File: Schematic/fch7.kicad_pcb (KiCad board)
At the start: 4 copper layers, 39.8 x 41.5 mm, 145 parts, among them IC1 MP9943AGQ-Z, IC2 MP9943AGQ-Z, IC4 ICM-42688-P, IC5 MPU-6500, J11 PIN2216, J12 PIN2216, J2 PIN2216, J3 PIN2216, J4 PIN2216, J5 PIN2216, J6 PIN2216, J7 PIN2216, J8 PIN2216, J9 PIN2216, U1 ME6217C33M5G, U10 HDGC1002WR-S-4P, U11 HDGC1002WR-S-4P, U12 E28-2G4M27SX, U13 STM32H742VIHx, U15 HDGC1002WR-S-6P, U16 HDGC1002WR-S-8P, U17 HDGC1002WR-S-8P, U2 ME6217C33M5G, U3 LDO-1.8v, U4 QMC5883L, U5 SPL06-001, U6 CSNP1GCR01-BOW, U7 HDGC1002WR-S-6P, U8 HDGC1002WR-S-4P, U9 HDGC1002WR-S-4P, Y1 8MHz

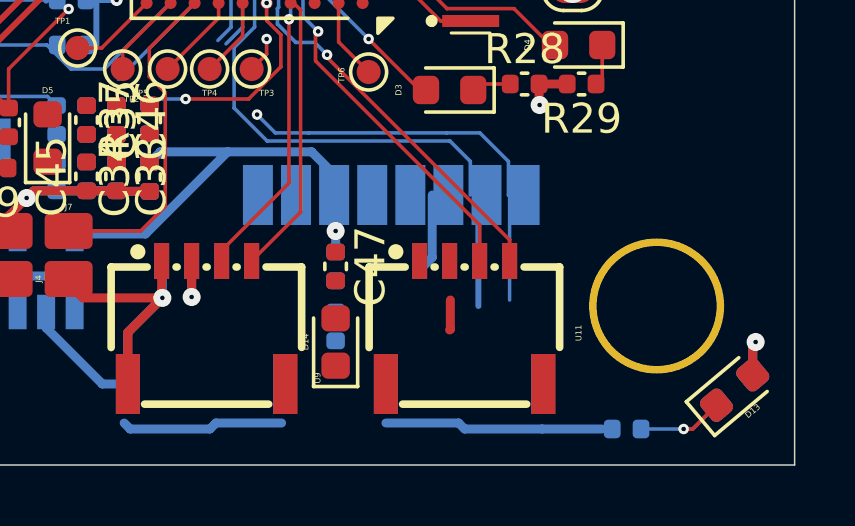
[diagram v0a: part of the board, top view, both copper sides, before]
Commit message: Update schematic files and footprint references
- Updated the footprint reference in `fp-info-cache` for various components to use "fch7" instead of "fch7_fp".
- Added a new 3D library reference for "fch7_3d" in `fp-lib-table`.
- Introduced a new symbol for the RF GPS module "MIA-M10Q" in `rf_rx.kicad_sch`, including properties such as footprint, datasheet, and description.
- Added multiple pins for the "MIA-M10Q" symbol with unique UUIDs.
- Corrected the URI for the `fclib` in `sym-lib-table` to point to the correct project path.
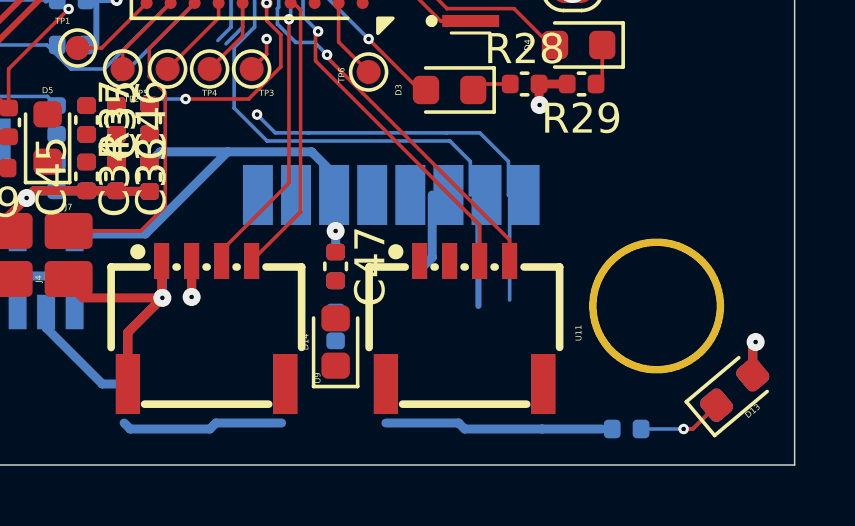
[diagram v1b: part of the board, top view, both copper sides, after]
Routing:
- net 5V: track 37.2 -> 36.2 mm
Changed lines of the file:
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@@
-	)
-	(segment
-		(start 92.724967 97.175033)
-		(end 92.7 97.2)
-		(width 0.3)
-		(layer "F.Cu")
-		(net 9)
 	)
 	(segment
@@
 		(layer "F.Cu")
 		(net 9)
-	)
-	(segment
-		(start 92.724967 96.2)
-		(end 92.724967 97.175033)
-		(width 0.3)
-		(layer "F.Cu")
-		(net 9)

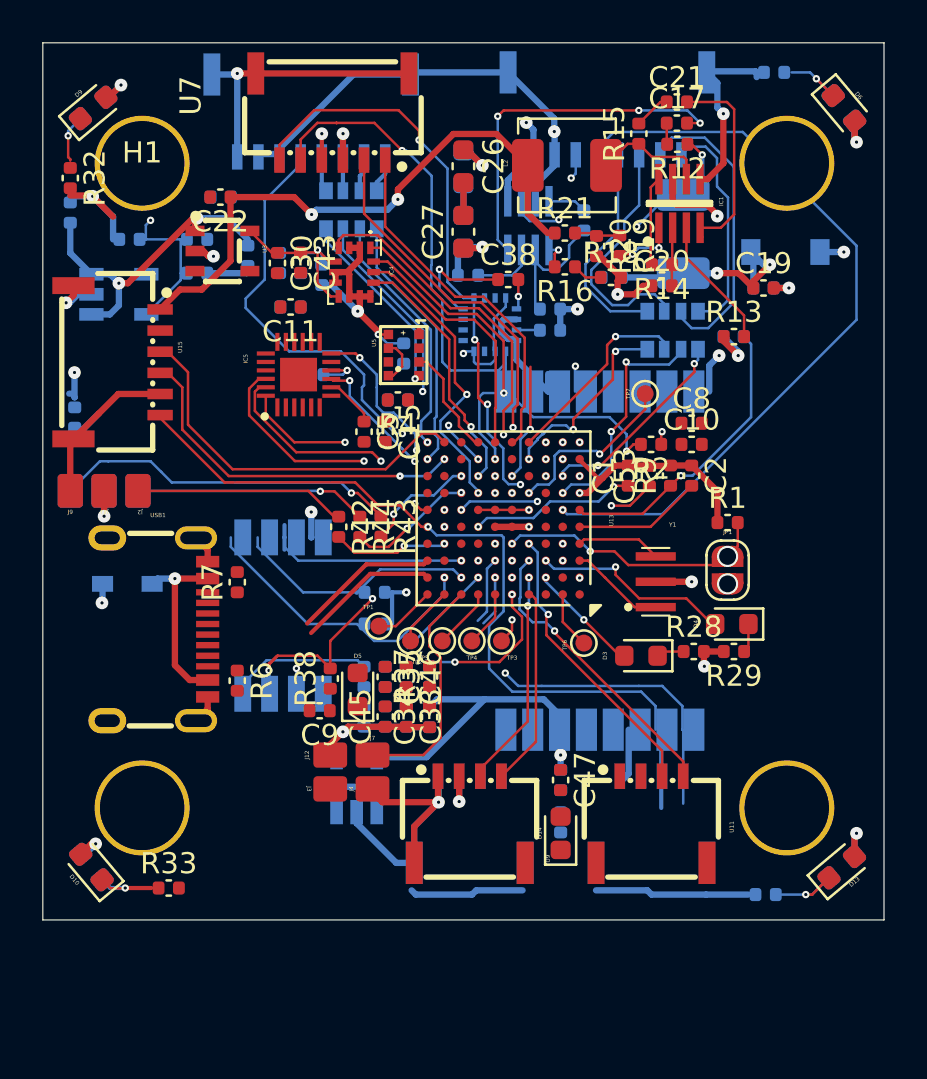
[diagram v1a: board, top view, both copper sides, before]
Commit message: update routing and add MIA-M10Q
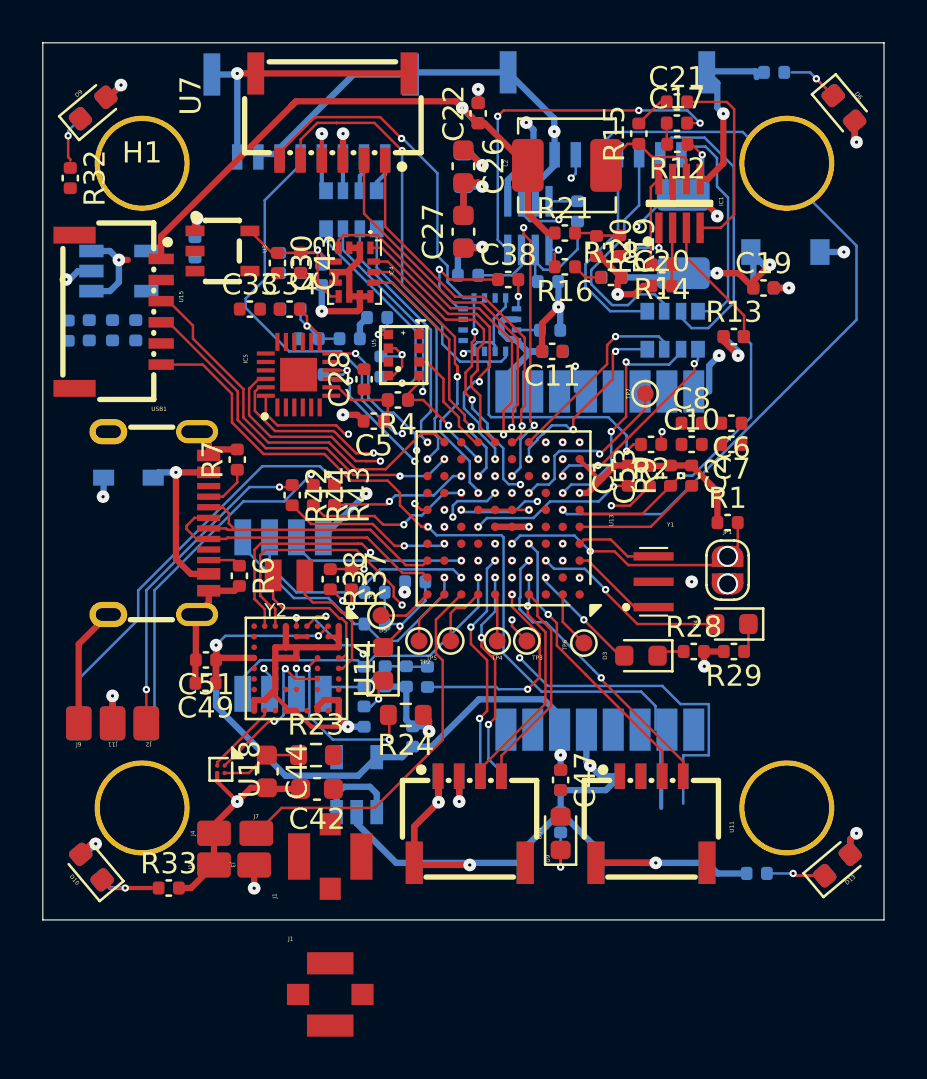
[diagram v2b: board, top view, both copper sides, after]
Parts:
- added C42: DNP, Capacitor_SMD:C_0603_1608Metric, F.Cu at (77.4, 95.5)
- added C44: DNP, Capacitor_SMD:C_0603_1608Metric, F.Cu at (75.0, 94.7)
- added C49: 10u, Capacitor_SMD:C_0402_1005Metric, F.Cu at (72.1, 90.5)
- added C51: 0.1u, Capacitor_SMD:C_0402_1005Metric, F.Cu at (72.1, 89.4)
- added J1: Conn_Coaxial, fch7:AMPHENOL_A-1JB, F.Cu at (78.0, 105.2)
- added J1: A-1JB, fch7:AMPHENOL_A-1JB, F.Cu at (78.0, 98.7)
- added R23: 0, Resistor_SMD:R_0603_1608Metric, F.Cu at (77.3, 93.9)
- added R24: 10k, Resistor_SMD:R_0603_1608Metric, F.Cu at (81.6, 92.0)
- added U14: MIA-M10Q, Package_LGA:ublox_LGA-53_4.5x4.5mm_Layout9x9_P0.5mm, F.Cu at (76.4, 89.8)
- added U18: MAX40200ANS, Package_BGA:WLP-4_0.728x0.728mm_Layout2x2_P0.35mm, F.Cu at (72.8, 94.6)
- added Y2: CM8V-T1A, fch7:XTAL_CM8V-T1A-32.768KHZ-7PF-20PPM-TB-QC, F.Cu at (76.0, 85.4)
- C15, C35, C45, C46, C9: moved to B.Cu
- C28, C6, C7: moved to F.Cu
- moved C6 26.7 mm to (97.0, 78.2), turned to 180 degrees
- moved C7 26.5 mm to (97.0, 79.2), turned to 180 degrees
- moved C33 20.7 mm to (74.2, 72.8), turned to 0 degrees
- moved C34 20.4 mm to (76.1, 72.8), turned to 0 degrees
- moved C36 19.0 mm to (88.5, 74.8), turned to 0 degrees
- moved C37 16.4 mm to (77.0, 74.2), turned to 0 degrees
- moved C35 16.1 mm to (78.9, 74.2), turned to 180 degrees
- moved C28 16.1 mm to (79.6, 76.1), turned to 90 degrees
- moved C29 14.7 mm to (80.4, 75.5), turned to -90 degrees
- moved C15 13.8 mm to (67.7, 73.8)
- moved C22 12.8 mm to (85.0, 63.5), turned to 90 degrees
- moved C23 12.8 mm to (85.0, 63.5), turned to 90 degrees
- moved C11 12.6 mm to (88.5, 74.8)
- moved J11 11.0 mm to (67.7, 92.4)
- moved J2 11.0 mm to (69.3, 92.4)
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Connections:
- net Net-(D14-K) renamed /rf_rx/LED_RECV
- net Net-(D3-K) renamed /Blackbox_led/LED0_R
- net Net-(D4-K) renamed /Blackbox_led/LED1_R
- net Net-(D5-K) renamed /Blackbox_led/LED_MCU_R
- net Net-(IC5-REGOUT) renamed /Sensors/REGOUT
- net Net-(U4-SETC) renamed /Sensors/SETC
- net Net-(U4-SETP) renamed /Sensors/SETP
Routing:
- net GND: track 137.8 -> 177.7 mm, vias 20 -> 27
- net UART1_RX: track 17.3 -> 39.2 mm, vias 0 -> 2
- net UART1_TX: track 20.2 -> 40.2 mm, vias 2 -> 4
- net VDD_RECV: track 15.4 -> 34.2 mm, vias 1 -> 3
- net I2C1_SDA: track 40.5 -> 54.8 mm, vias 6 -> 7
- net I2C1_SCL: track 42.3 -> 55.9 mm, vias 3 -> 5
- net VDD_MCU: track 29.4 -> 40.6 mm, vias 9 -> 11
- net UART7_RX: track 6.84 -> 17.0 mm, vias 3 -> 4
- net 5V: track 36.2 -> 27.3 mm
- net /rf_rx/RESET_MIA: track 0.00 -> 8.44 mm, vias 0 -> 2
- net UART2_RX: track 3.19 -> 11.2 mm, vias 1 -> 3
- net UART2_TX: track 2.39 -> 10.3 mm, vias 1 -> 3
- net /rf_rx/VCC_RF: track 0.00 -> 7.74 mm, vias 0 -> 2
- net BEEPER: track 11.2 -> 18.3 mm
- net /MCU/OTG_FS+: track 6.79 -> 13.8 mm
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
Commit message: update routing
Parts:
- removed the J1 at (78.0, 105.2)
- removed the J1 at (78.0, 98.7)
- added J1: Conn_Coaxial, fch7:AMPHENOL_A-1JB, F.Cu at (78.2, 98.8)
- moved C29 0.60 mm to (81.0, 75.5), turned to 0 degrees
- moved R22 0.42 mm to (79.8, 73.2)
- moved C32 0.41 mm to (77.6, 75.8)
- moved D6 0.37 mm to (102.0, 63.1)
- moved D7 0.36 mm to (102.0, 63.1)
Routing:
- net GND: track 177.7 -> 238.2 mm, vias 27 -> 31
- net VDD_MCU: track 40.6 -> 57.7 mm, vias 11 -> 16
- net BEEPER: track 18.3 -> 7.61 mm
- net 5V: track 27.3 -> 33.5 mm, vias 12 -> 15
- net /rf_rx/RF_IN: track 0.00 -> 3.80 mm
- net VDD_RECV: track 34.2 -> 37.7 mm
- net I2C2_SDA: track 5.26 -> 7.43 mm, vias 0 -> 1
- net UART6_RX: track 39.0 -> 37.1 mm
- net NRESET_RECV: track 18.3 -> 20.1 mm
- net Net-(D8-K): track 2.27 -> 3.66 mm
- net UART6_TX: track 27.2 -> 28.2 mm
- net VCC_ICM: track 9.36 -> 10.4 mm
- net SENS_CUR1: track 36.4 -> 37.2 mm
- net SPI4_SCLK: track 14.4 -> 13.6 mm
- net Net-(R16-Pad1): track 1.23 -> 1.97 mm, vias 0 -> 1
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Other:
- board size 39.8 x 41.5 mm -> 39 x 40.9 mm

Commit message: update routing
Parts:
- J1: value Conn_Coaxial -> U.FL-R-SMT-1_01_; footprint fch7:AMPHENOL_A-1JB -> fch7:HIROSE_U.FL-R-SMT-1_01_
- moved J1 0.21 mm to (78.1, 98.6), turned to 180 degrees
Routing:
- net GND: track 238.2 -> 251.1 mm
- net /rf_rx/RF_IN: track 3.80 -> 5.39 mm

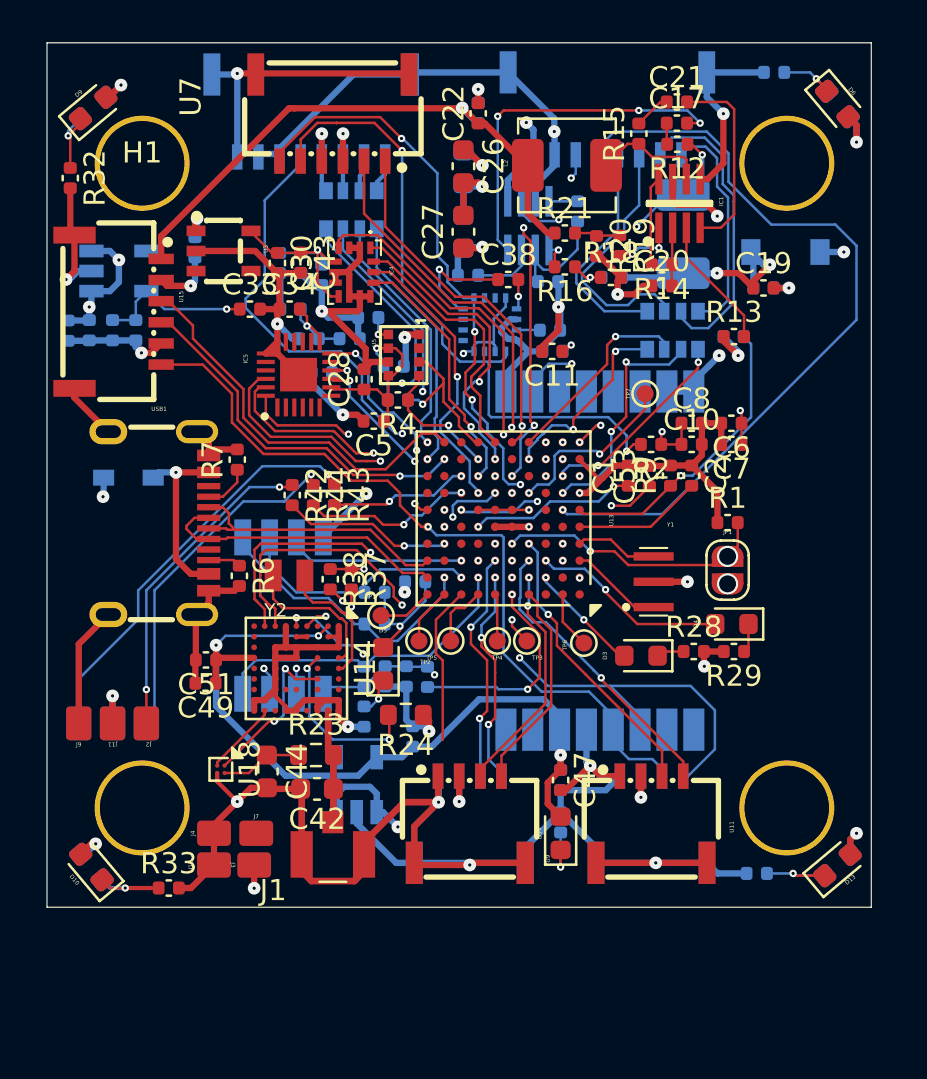
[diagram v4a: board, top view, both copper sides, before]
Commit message: fix: update library URI for fch7 footprint in fp-lib-table
Changed the URI for the fch7 library from a relative path to a defined variable for better path management. This improves the portability of the project across different environments.
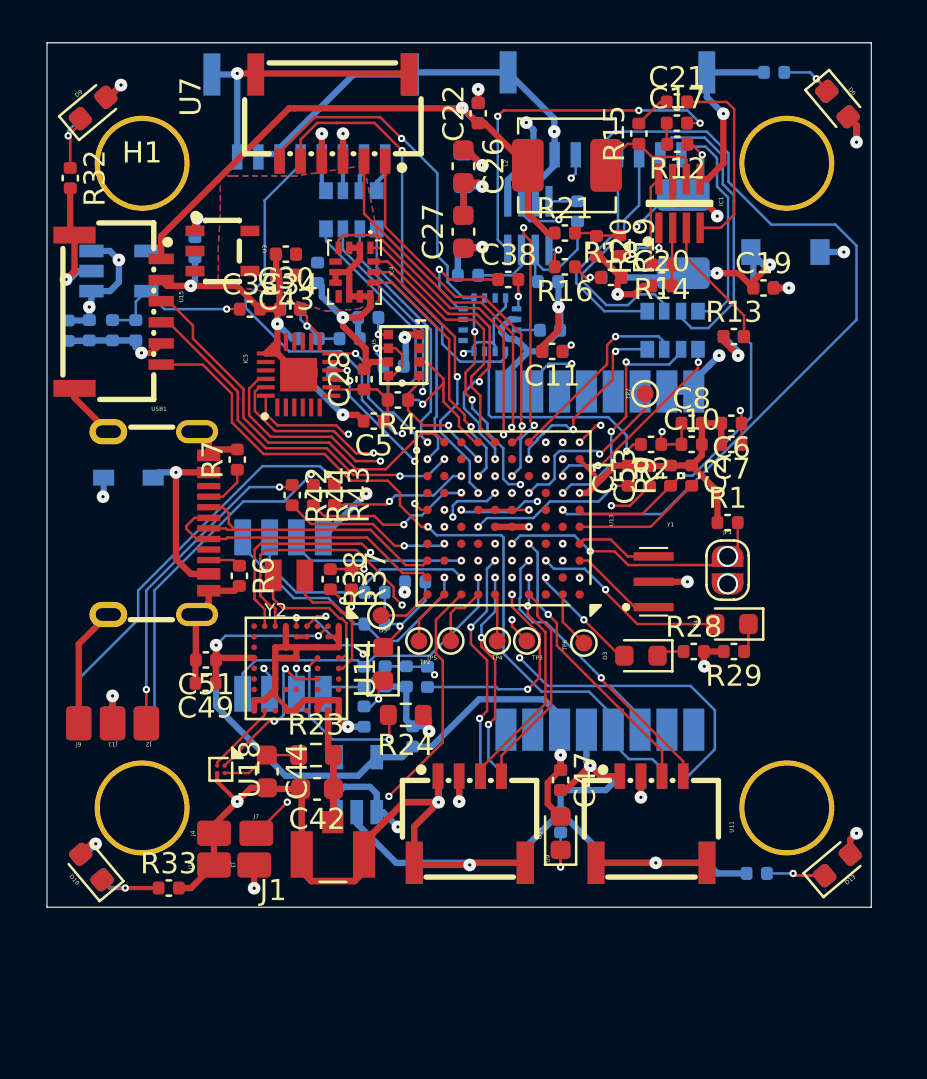
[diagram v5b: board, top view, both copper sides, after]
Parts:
- moved C41 0.91 mm to (75.9, 71.2), turned to 0 degrees
- moved C43 0.91 mm to (75.9, 71.2), turned to 180 degrees
- moved C30 0.58 mm to (75.9, 70.2), turned to 180 degrees
- moved C4 0.52 mm to (75.9, 70.2), turned to 180 degrees
- moved C40 0.22 mm to (77.4, 71.1)
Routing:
- net BEEPER: track 7.61 -> 18.3 mm, vias 0 -> 2
- net VCC_ICM: track 10.4 -> 0.03 mm, vias 1 -> 0
- net GND: track 251.1 -> 244.9 mm
- added copper zone on B.Cu, net VCC_ICM
- added copper zone on F.Cu, net VCC_ICM
- removed copper zone on In2.Cu, net VCC_ICM

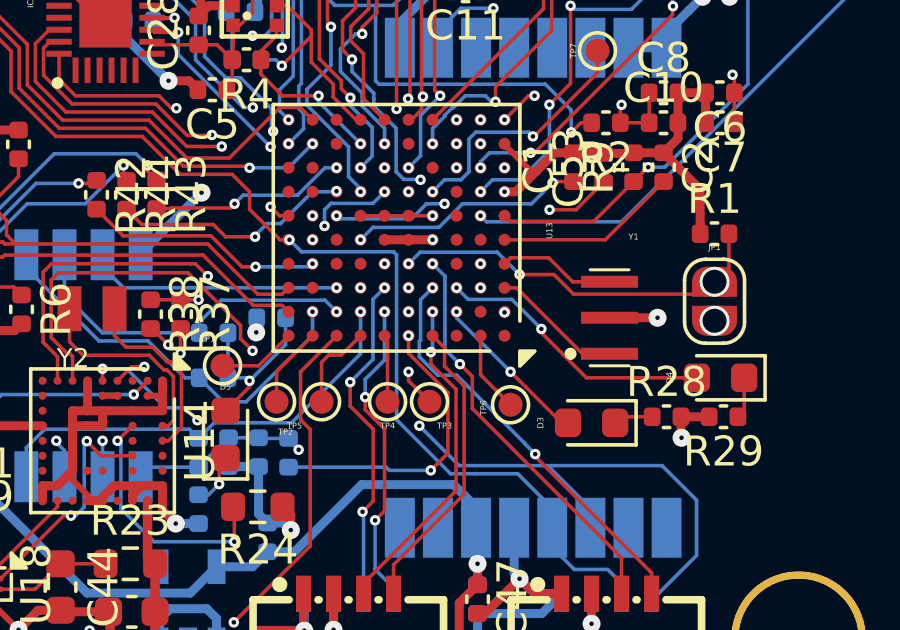
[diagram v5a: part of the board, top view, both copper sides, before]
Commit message: Fix junction and wire positions in schematic; update capacitor and ground symbol properties
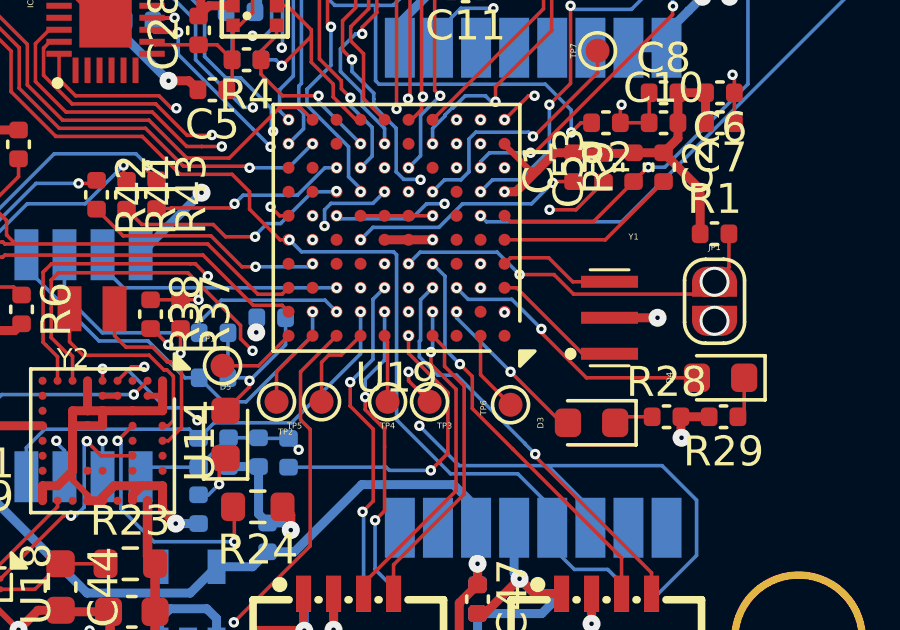
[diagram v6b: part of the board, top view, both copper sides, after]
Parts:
- removed U13: STM32H742VIHx, Package_BGA:TFBGA-100_8x8mm_Layout10x10_P0.8mm
- added U19: STM32H743VIHx, Package_BGA:TFBGA-100_8x8mm_Layout10x10_P0.8mm, F.Cu at (86.2, 82.7)
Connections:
- U14 pad D1: I2C1_SDA -> unconnected-(U14-SDA-PadD1)
- U14 pad E1: I2C1_SCL -> unconnected-(U14-SCL-PadE1)

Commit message: Minor refactor
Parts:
- moved C12 1.40 mm to (67.0, 73.7)
- moved C13 1.40 mm to (68.0, 73.7)
- moved C15 1.30 mm to (69.0, 73.7)
- moved C14 1.20 mm to (70.0, 73.7)
- moved U2 0.70 mm to (68.7, 71.0)
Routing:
- net VCC_ICM: track 0.03 -> 4.22 mm, vias 0 -> 2
- net GND: track 244.9 -> 248.5 mm
- net VDD_MCU: track 57.7 -> 56.3 mm
- net I2C1_SDA: track 54.8 -> 53.7 mm
- net 5V: track 33.5 -> 34.3 mm, vias 15 -> 14
- net I2C1_SCL: track 55.9 -> 55.5 mm, vias 5 -> 4
